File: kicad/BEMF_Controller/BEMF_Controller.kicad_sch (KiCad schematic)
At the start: 96 parts, among them J1 HEADER4VALULOK, J2 HEADER6, J3 FUSE, J4 Coil_A, J5 Coil_B, J6 Coil_C, Q1 IGBT-TO-247, Q2 IGBT-TO-247, Q3 IGBT-TO-247, Q4 IGBT-TO-247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

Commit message: Fixed two errors
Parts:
- D40: value MBRB20300S -> V10P15-M3/H
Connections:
- net 5V: now also D50.1 (K), D53.1 (K), D57.1 (K)
- net OVP_A: no longer C42.1, D57.2 (A), D58.1 (K), R24.2, R25.1
- net OVP_C: now also C42.1, D57.2 (A), D58.1 (K), R24.2, R25.1
- net at D56.2 (A), R24.1: no longer D57.1 (K)
- net at D48.2 (A), R20.1: no longer D50.1 (K)
- net at D52.2 (A), R22.1: no longer D53.1 (K)
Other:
- moved on the sheet: D47, D48, D51, D52, D55, D56

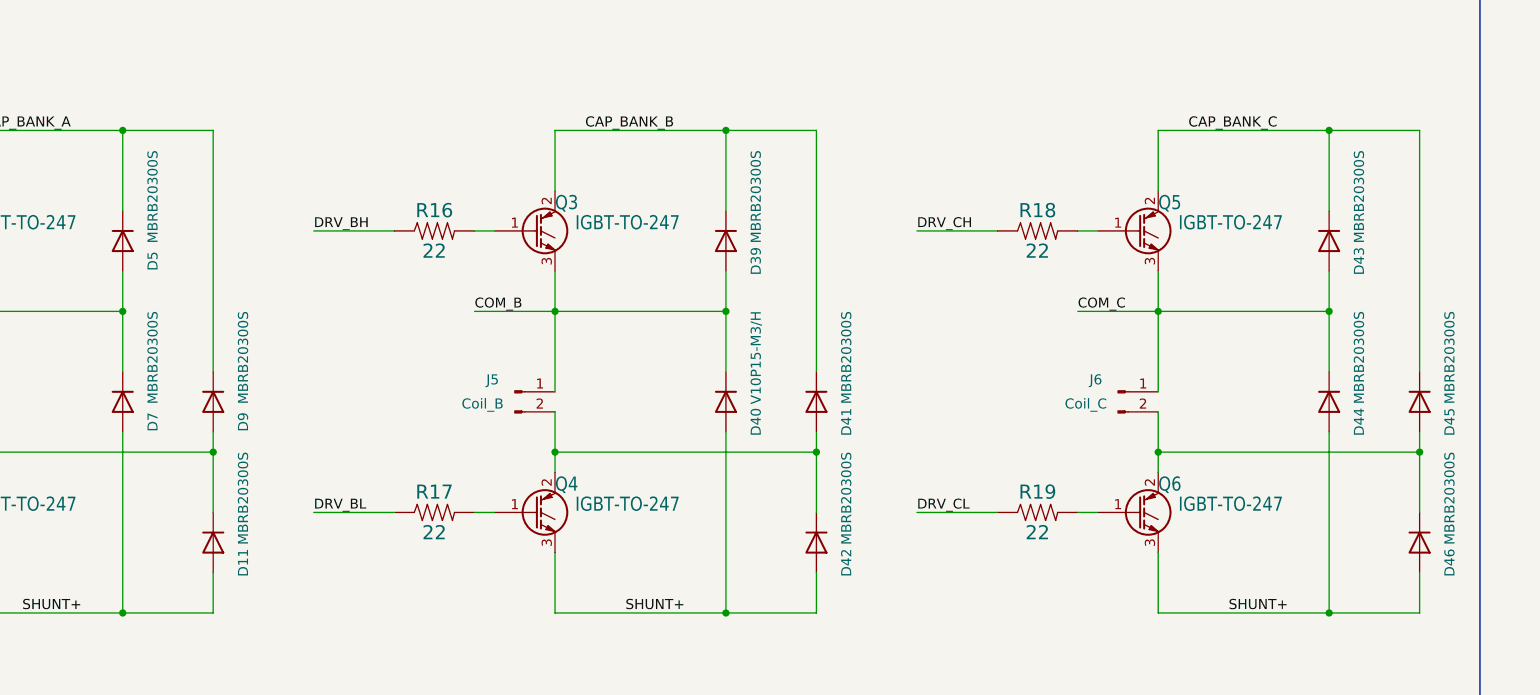
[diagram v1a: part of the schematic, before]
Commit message: replaced shottky diodes
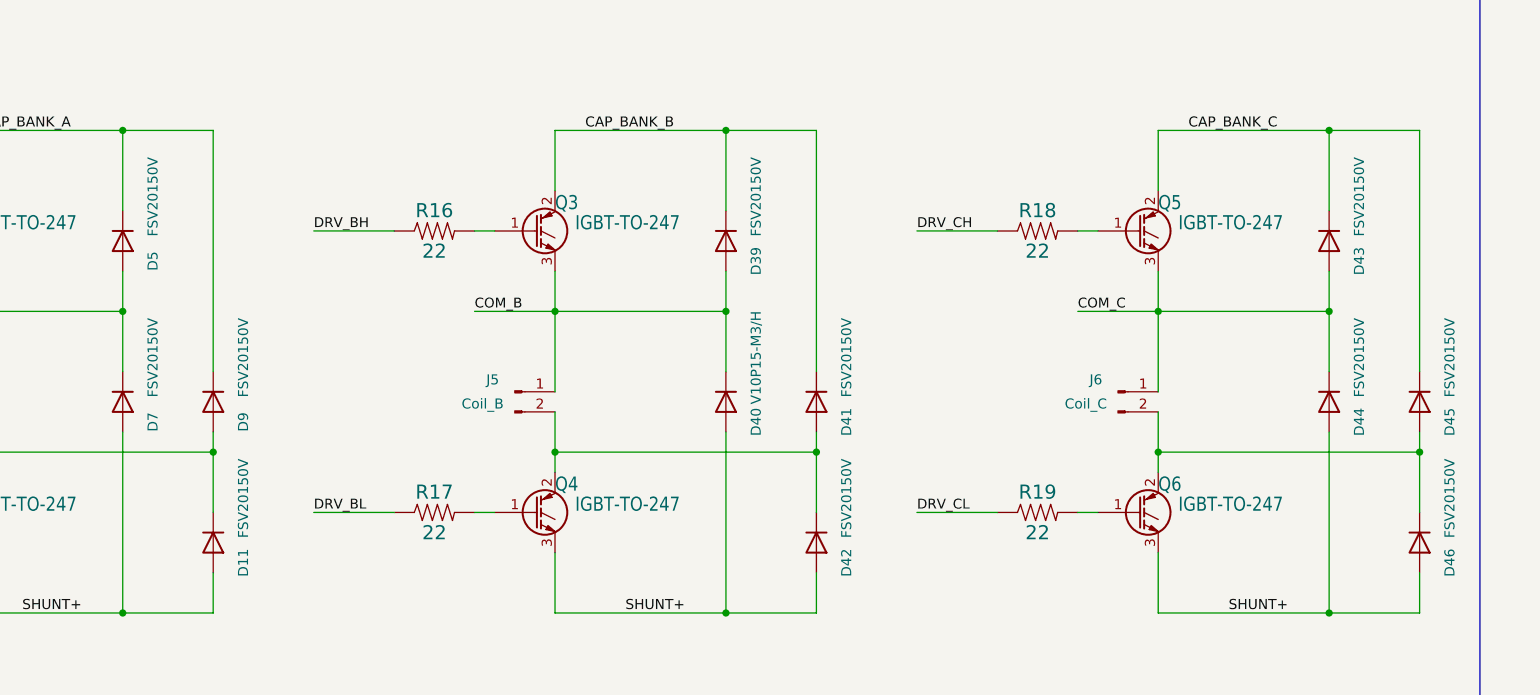
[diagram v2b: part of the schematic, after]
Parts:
- D11, D39, D41, D42, D43, D44, D45, D46, D5, D7, D9: value MBRB20300S -> FSV20150V; footprint Package_TO_SOT_SMD:TO-263-2 -> Package_TO_SOT_SMD:TO-277A
- D40: footprint Package_TO_SOT_SMD:TO-263-2 -> Package_TO_SOT_SMD:TO-277A
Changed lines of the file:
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@@
 			)
 		)
-		(property "Value" "MBRB20300S"
+		(property "Value" "FSV20150V"
 			(at 229.87 121.412 0)
 			(effects
@@
 			)
 		)
-		(property "Footprint" "Package_TO_SOT_SMD:TO-263-2"
+		(property "Footprint" "Package_TO_SOT_SMD:TO-277A"
 			(at 226.06 127 0)
 			(effects
@@
 			)
 		)
-		(property "Value" "MBRB20300S"
+		(property "Value" "FSV20150V"
 			(at 241.3 159.512 0)
 			(effects
@@
 			)
 		)
-		(property "Footprint" "Package_TO_SOT_SMD:TO-263-2"
+		(property "Footprint" "Package_TO_SOT_SMD:TO-277A"
 			(at 237.49 165.1 0)
 			(effects
@@
 			)
 		)
-		(property "Value" "MBRB20300S"
+		(property "Value" "FSV20150V"
 			(at 317.5 141.732 0)
 			(effects
@@
 			)
 		)
-		(property "Footprint" "Package_TO_SOT_SMD:TO-263-2"
+		(property "Footprint" "Package_TO_SOT_SMD:TO-277A"
 			(at 313.69 147.32 0)
 			(effects
@@
 			)
 		)
-		(property "Value" "MBRB20300S"
+		(property "Value" "FSV20150V"
 			(at 382.27 121.412 0)
 			(effects
@@
 			)
 		)
-		(property "Footprint" "Package_TO_SOT_SMD:TO-263-2"
+		(property "Footprint" "Package_TO_SOT_SMD:TO-277A"
 			(at 378.46 127 0)
 			(effects
@@
 			)
 		)
-		(property "Value" "MBRB20300S"
+		(property "Value" "FSV20150V"
 			(at 382.27 141.732 0)
 			(effects
@@
 			)
 		)
-		(property "Footprint" "Package_TO_SOT_SMD:TO-263-2"
+		(property "Footprint" "Package_TO_SOT_SMD:TO-277A"
 			(at 378.46 147.32 0)
 			(effects
@@
 			)
 		)
-		(property "Value" "MBRB20300S"
+		(property "Value" "FSV20150V"
 			(at 393.7 141.732 0)
 			(effects
@@
 			)
 		)
-		(property "Footprint" "Package_TO_SOT_SMD:TO-263-2"
+		(property "Footprint" "Package_TO_SOT_SMD:TO-277A"
 			(at 389.89 147.32 0)
 			(effects
@@
 			)
 		)
-		(property "Value" "MBRB20300S"
+		(property "Value" "FSV20150V"
 			(at 317.5 159.512 0)
 			(effects
@@
 			)
 		)
-		(property "Footprint" "Package_TO_SOT_SMD:TO-263-2"
+		(property "Footprint" "Package_TO_SOT_SMD:TO-277A"
 			(at 313.69 165.1 0)
 			(effects
@@
 			)
 		)
-		(property "Value" "MBRB20300S"
+		(property "Value" "FSV20150V"
 			(at 393.7 159.512 0)
 			(effects
@@
 			)
 		)
-		(property "Footprint" "Package_TO_SOT_SMD:TO-263-2"
+		(property "Footprint" "Package_TO_SOT_SMD:TO-277A"
 			(at 389.89 165.1 0)
 			(effects
@@
 			)
 		)
-		(property "Value" "MBRB20300S"
+		(property "Value" "FSV20150V"
 			(at 241.3 141.732 0)
 			(effects
@@
 			)
 		)
-		(property "Footprint" "Package_TO_SOT_SMD:TO-263-2"
+		(property "Footprint" "Package_TO_SOT_SMD:TO-277A"
 			(at 237.49 147.32 0)
 			(effects
@@
 			)
 		)
-		(property "Value" "MBRB20300S"
+		(property "Value" "FSV20150V"
 			(at 229.87 141.732 0)
 			(effects
@@
 			)
 		)
-		(property "Footprint" "Package_TO_SOT_SMD:TO-263-2"
+		(property "Footprint" "Package_TO_SOT_SMD:TO-277A"
 			(at 226.06 147.32 0)
 			(effects
@@
 			)
 		)
-		(property "Value" "MBRB20300S"
+		(property "Value" "FSV20150V"
 			(at 306.07 121.412 0)
 			(effects
@@
 			)
 		)
-		(property "Footprint" "Package_TO_SOT_SMD:TO-263-2"
+		(property "Footprint" "Package_TO_SOT_SMD:TO-277A"
 			(at 302.26 127 0)
 			(effects
@@
 			)
 		)
-		(property "Footprint" "Package_TO_SOT_SMD:TO-263-2"
+		(property "Footprint" "Package_TO_SOT_SMD:TO-277A"
 			(at 302.26 147.32 0)
 			(effects

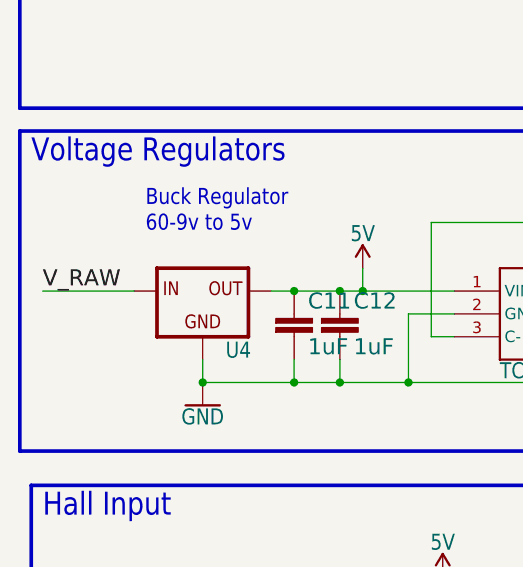
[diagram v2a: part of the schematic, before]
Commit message: Detach controller power supply from power section.
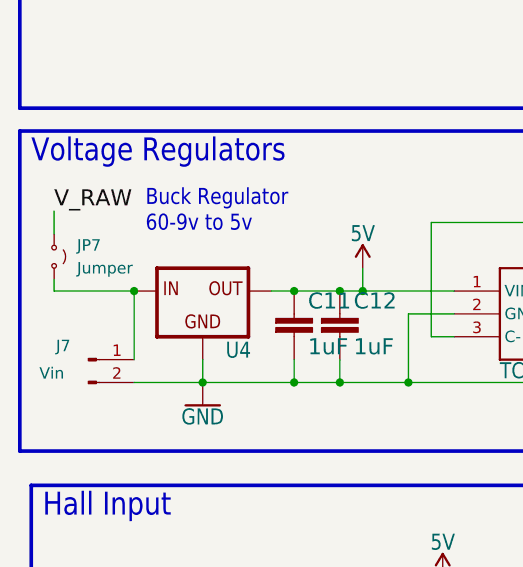
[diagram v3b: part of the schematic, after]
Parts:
- added J7: Vin, TerminalBlock_Phoenix:TerminalBlock_Phoenix_MKDS-1,5-2-5.08_1x02_P5.08mm_Horizontal, symbol Connector:Conn_01x02_Pin
- added JP7: Jumper, Connector_PinHeader_2.54mm:PinHeader_1x02_P2.54mm_Vertical, symbol Jumper:Jumper_2_Small_Open
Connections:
- net GND: now also J7.2 (Pin_2)
- net V_RAW: now also JP7.1 (A); no longer U4.IN
- new net: J7.1 (Pin_1), JP7.2 (B), U4.IN
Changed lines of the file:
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@@
 	)
 	(junction
+		(at 21.59 107.95)
+		(diameter 0)
+		(color 0 0 0 0)
+	)
+	(junction
 		(at 213.36 54.61)
 		(diameter 0)
@@
 	(wire
 		(pts
+			(xy 12.7 99.06) (xy 12.7 101.6)
+		)
+		(stroke
+			(width 0)
+			(type default)
+		)
+	)
+	(wire
+		(pts
 			(xy 342.9 50.8) (xy 325.12 50.8)
 		)
@@
 	(wire
 		(pts
+			(xy 21.59 118.11) (xy 29.21 118.11)
+		)
+		(stroke
+			(width 0)
+			(type default)
+		)
+	)
+	(wire
+		(pts
 			(xy 172.72 21.59) (xy 175.26 21.59)
 		)
@@
 	(wire
 		(pts
+			(xy 21.59 107.95) (xy 21.59 115.57)
+		)
+		(stroke
+			(width 0)
+			(type default)
+		)
+	)
+	(wire
+		(pts
 			(xy 213.36 54.61) (xy 220.98 54.61)
 		)
@@
 	(wire
 		(pts
+			(xy 12.7 106.68) (xy 12.7 107.95)
+		)
+		(stroke
+			(width 0)
+			(type default)
+		)
+	)
+	(wire
+		(pts
 			(xy 59.69 59.69) (xy 72.39 59.69)
 		)
@@
 	(wire
 		(pts
-			(xy 21.59 107.95) (xy 11.43 107.95)
-		)
-		(stroke
-			(width 0.1524)
-			(type solid)
-		)
-	)
-	(wire
-		(pts
 			(xy 302.26 130.81) (xy 302.26 135.89)
 		)
@@
 	(wire
 		(pts
+			(xy 12.7 107.95) (xy 21.59 107.95)
+		)
+		(stroke
+			(width 0)
+			(type default)
+		)
+	)
+	(wire
+		(pts
 			(xy 182.88 44.45) (xy 182.88 54.61)
 		)
@@
 	)
 	(label "V_RAW"
-		(at 11.43 107.95 0)
+		(at 12.7 99.06 0)
 		(fields_autoplaced yes)
 		(effects
@@
 	)
 	(symbol
+		(lib_id "Connector:Conn_01x02_Pin")
+		(at 16.51 115.57 0)
+		(unit 1)
+		(exclude_from_sim no)
+		(in_bom yes)
+		(on_board yes)
+		(dnp no)
+		(property "Reference" "J7"
+			(at 13.716 114.046 0)
+			(effects
+				(font
+					(size 1.27 1.27)
+				)
+			)
+		)
+		(property "Value" "Vin"
+			(at 12.446 117.094 0)
+			(effects
+				(font
+					(size 1.27 1.27)
+				)
+			)
+		)
+		(property "Footprint" "TerminalBlock_Phoenix:TerminalBlock_Phoenix_MKDS-1,5-2-5.08_1x02_P5.08mm_Horizontal"
+			(at 16.51 115.57 0)
+			(effects
+				(font
+					(size 1.27 1.27)
+				)
+				(hide yes)
+			)
+		)
+		(property "Datasheet" "~"
+			(at 16.51 115.57 0)
+			(effects
+				(font
+					(size 1.27 1.27)
+				)
+				(hide yes)
+			)
+		)
+		(property "Description" "Generic connector, single row, 01x02, script generated"
+			(at 16.51 115.57 0)
+			(effects
+				(font
+					(size 1.27 1.27)
+				)
+				(hide yes)
+			)
+		)
+		(pin "2"
+		)
+		(pin "1"
+		)
+		(instances
+			(project "BEMF_Controller"
+				(path "/80a514a6-29a9-4699-8a7d-cff678a7ed07"
+					(reference "J7")
+					(unit 1)
+				)
+			)
+		)
+	)
+	(symbol
 		(lib_id "main-eagle-import:1.0UF-1206-50V-10%")
 		(at 44.45 113.03 0)
@@
 					(unit 1)
 				)
+			)
+		)
+	)
+	(symbol
+		(lib_id "Jumper:Jumper_2_Small_Open")
+		(at 12.7 104.14 270)
+		(unit 1)
+		(exclude_from_sim yes)
+		(in_bom yes)
+		(on_board yes)
+		(dnp no)
+		(fields_autoplaced yes)
+		(property "Reference" "JP7"
+			(at 15.24 102.8699 90)
+			(effects
+				(font
+					(size 1.27 1.27)
+				)
+				(justify left)
+			)
+		)
+		(property "Value" "Jumper"
+			(at 15.24 105.4099 90)
+			(effects
+				(font
+					(size 1.27 1.27)
+				)
+				(justify left)
+			)
+		)
+		(property "Footprint" "Connector_PinHeader_2.54mm:PinHeader_1x02_P2.54mm_Vertical"
+			(at 12.7 104.14 0)
+			(effects
+				(font
+					(size 1.27 1.27)
+				)
+				(hide yes)
+			)
+		)
+		(property "Datasheet" "~"
+			(at 12.7 104.14 0)
+			(effects
+				(font
+					(size 1.27 1.27)
+				)
+				(hide yes)
+			)
+		)
+		(property "Description" "Jumper, 2-pole, small symbol, open"
+			(at 12.7 104.14 0)
+			(effects
+				(font
+					(size 1.27 1.27)
+				)
+				(hide yes)
+			)
+		)
+		(pin "1"
+		)
+		(pin "2"
+		)
+		(instances
+			(project "BEMF_Controller"
+				(path "/80a514a6-29a9-4699-8a7d-cff678a7ed07"
+					(reference "JP7")
+					(unit 1)
+				)

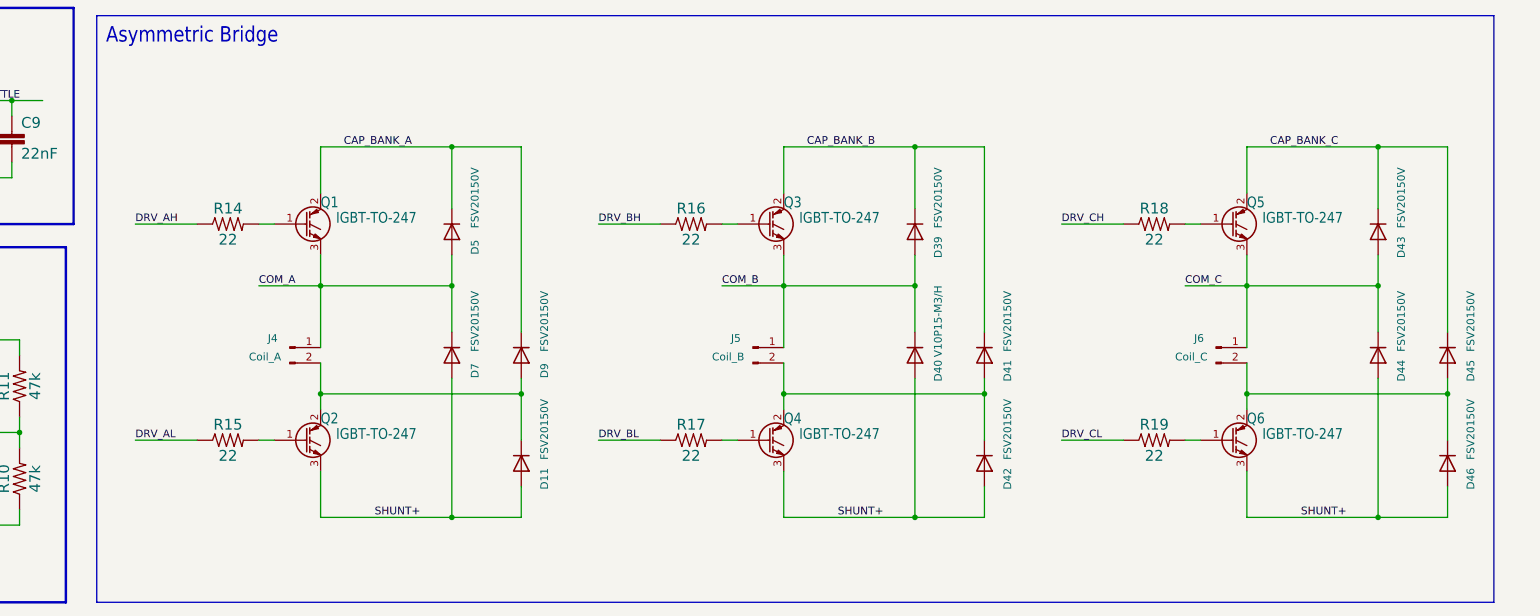
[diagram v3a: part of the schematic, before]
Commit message: Added diode and resistors to gate drive for faster switch off
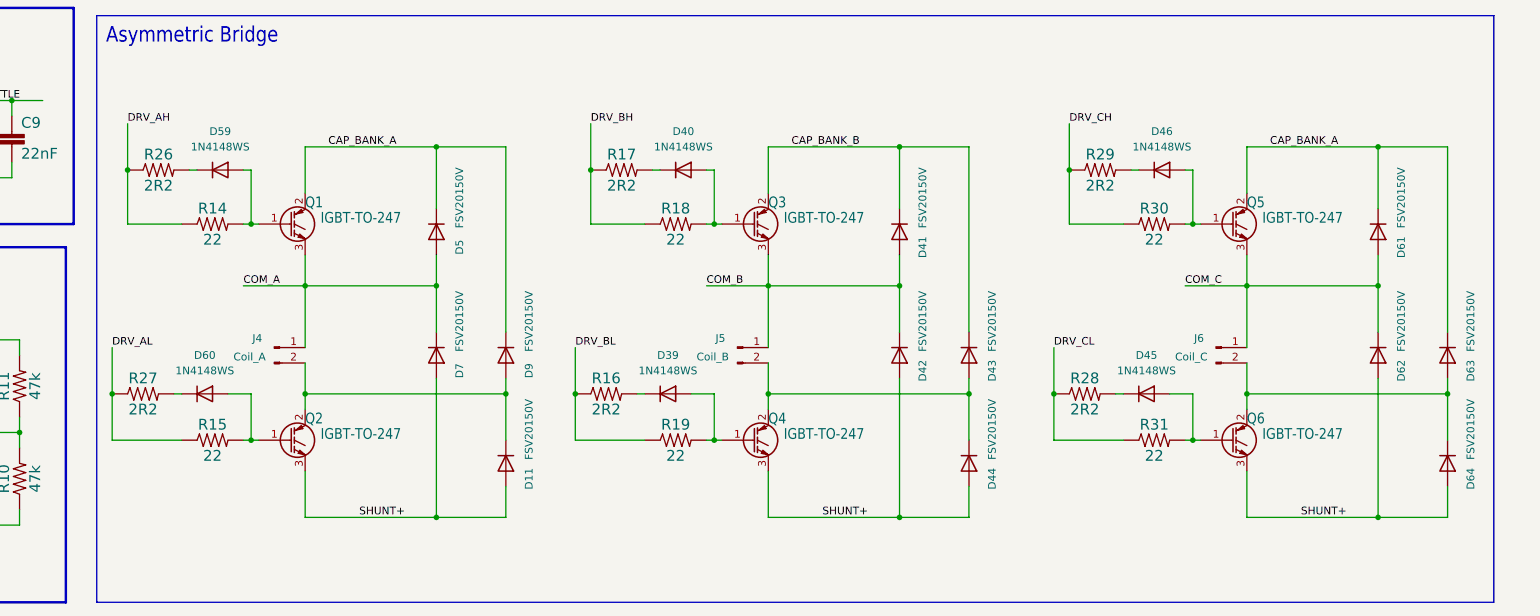
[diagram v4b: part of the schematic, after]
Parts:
- added D59, D60: 1N4148WS, Diode_SMD:D_SOD-323F, symbol Device:D
- added D61, D62, D63, D64: FSV20150V, Package_TO_SOT_SMD:TO-277A, symbol Device:D
- added R26, R27, R28, R29: 2R2, main:1206, symbol main-eagle-import:RESISTOR1206
- added R30, R31: 22, main:1206, symbol main-eagle-import:RESISTOR1206
- D39, D45, D46: value FSV20150V -> 1N4148WS; footprint Package_TO_SOT_SMD:TO-277A -> Diode_SMD:D_SOD-323F
- D40: value V10P15-M3/H -> 1N4148WS; footprint Package_TO_SOT_SMD:TO-277A -> Diode_SMD:D_SOD-323F
- R16, R17: value 22 -> 2R2
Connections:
- net CAP_BANK_A: now also Q5.2 (C), D61.1 (K), D63.1 (K)
- net CAP_BANK_B: now also D43.1 (K); no longer D39.1 (K)
- net CAP_BANK_C: no longer D43.1 (K), D45.1 (K), Q5.2 (C)
- net COM_B: now also D41.2 (A), D42.1 (K); no longer D39.2 (A), D40.1 (K)
- net COM_C: now also D61.2 (A), D62.1 (K); no longer D43.2 (A), D44.1 (K)
- net DRV_AH: now also R26.1
- net DRV_AL: now also R27.1
- net DRV_BH: now also R17.1, R18.1; no longer R16.1
- net DRV_BL: now also R16.1, R19.1; no longer R17.1
- net DRV_CH: now also R29.1, R30.1; no longer R18.1
- net DRV_CL: now also R28.1, R31.1; no longer R19.1
- net SHUNT+: now also D62.2 (A), D64.2 (A); no longer D40.2 (A), D46.2 (A)
- net at R18.2: now also D40.2 (A), Q3.1 (G); no longer Q5.1 (G)
- net at Q2.1 (G), R15.2: now also D60.2 (A)
- net at Q1.1 (G), R14.2: now also D59.2 (A)
- net at J5.2 (Pin_2), Q4.2 (C): now also D43.2 (A), D44.1 (K); no longer D41.2 (A), D42.1 (K)
- net at R17.2: now also D40.1 (K); no longer Q4.1 (G)
- net at R19.2: now also D39.2 (A), Q4.1 (G); no longer Q6.1 (G)
- net at J6.2 (Pin_2), Q6.2 (C): now also D63.2 (A), D64.1 (K); no longer D45.2 (A), D46.1 (K)
- net at R16.2: now also D39.1 (K); no longer Q3.1 (G)
- new net: D46.1 (K), R29.2
- new net: D46.2 (A), Q5.1 (G), R30.2
- new net: D60.1 (K), R27.2
- new net: D59.1 (K), R26.2
- new net: D45.2 (A), Q6.1 (G), R31.2
- new net: D45.1 (K), R28.2
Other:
- moved on the sheet: D11, D5, D7, D9, J4, Q1, Q2, R14, R15

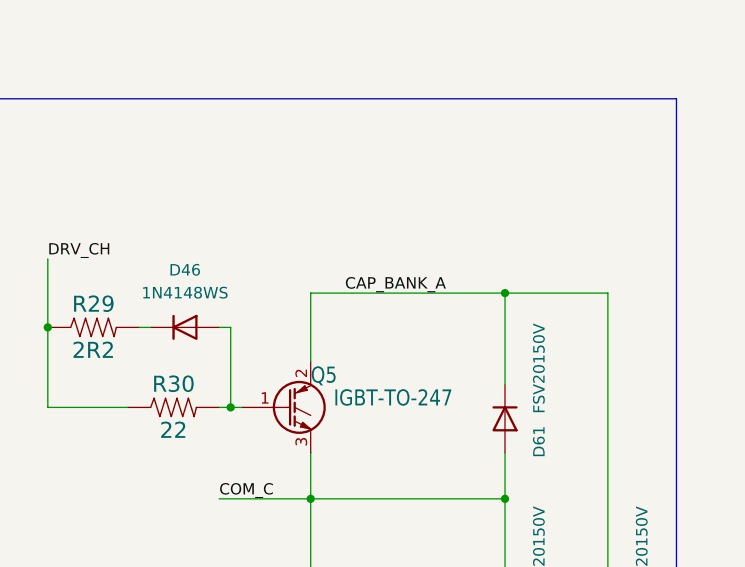
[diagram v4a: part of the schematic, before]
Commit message: Typo. Cap_bank_a label still on driver for bank c
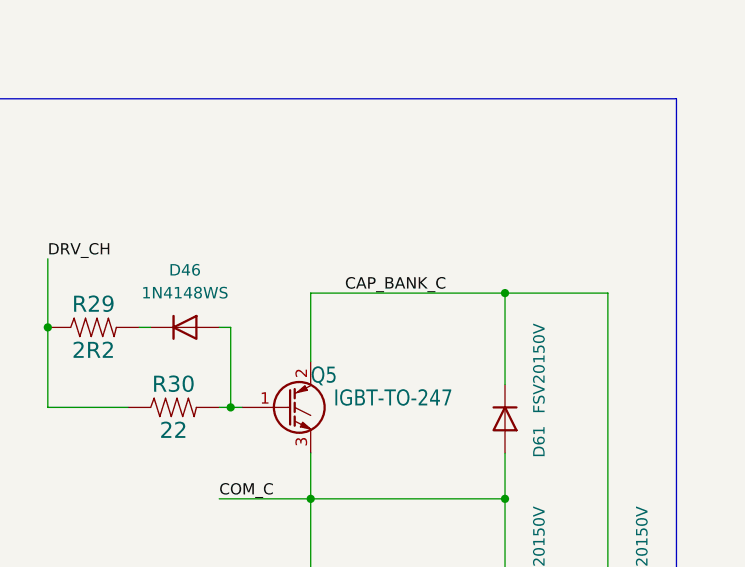
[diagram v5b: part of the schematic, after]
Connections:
- net CAP_BANK_A: no longer D61.1 (K), D63.1 (K), Q5.2 (C)
- net CAP_BANK_C: now also D61.1 (K), D63.1 (K), Q5.2 (C)
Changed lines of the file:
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@@
 		)
 	)
-	(label "CAP_BANK_A"
+	(label "CAP_BANK_C"
 		(at 360.68 113.03 0)
 		(fields_autoplaced yes)
